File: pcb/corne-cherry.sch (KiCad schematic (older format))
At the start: 146 parts, among them J1 MJ-4PP-9, J2 OLED, J3 MJ-4PP-9, J4 OLED, J5 Conn_01x01_Male, J6 Conn_01x01_Male, P1 Conn_01x03, P3 Conn_01x03, SW1 SW_PUSH, SW10 SW_PUSH, SW11 SW_PUSH, SW12 SW_PUSH, SW13 SW_PUSH, SW14 SW_PUSH, SW15 SW_PUSH, SW16 SW_PUSH, SW17 SW_PUSH, SW18 SW_PUSH, SW19 SW_PUSH, SW2 SW_PUSH, SW20 SW_PUSH, SW21 SW_PUSH, SW22 SW_PUSH, SW23 SW_PUSH, SW24 SW_PUSH, SW25 SW_PUSH, SW26 SW_PUSH, SW27 SW_PUSH, SW28 SW_PUSH, SW29 SW_PUSH, SW3 SW_PUSH, SW30 SW_PUSH, SW31 SW_PUSH, SW32 SW_PUSH, SW33 SW_PUSH, SW34 SW_PUSH, SW35 SW_PUSH, SW36 SW_PUSH, SW37 SW_PUSH, SW38 SW_PUSH, SW39 SW_PUSH, SW4 SW_PUSH, SW40 SW_PUSH, SW41 SW_PUSH, SW42 SW_PUSH, SW43 Rotary_Encoder_Switch, SW44 Rotary_Encoder_Switch, SW5 SW_PUSH, SW6 SW_PUSH, SW7 SW_PUSH, SW8 SW_PUSH, SW9 SW_PUSH, U1 ProMicro, U2 ProMicro

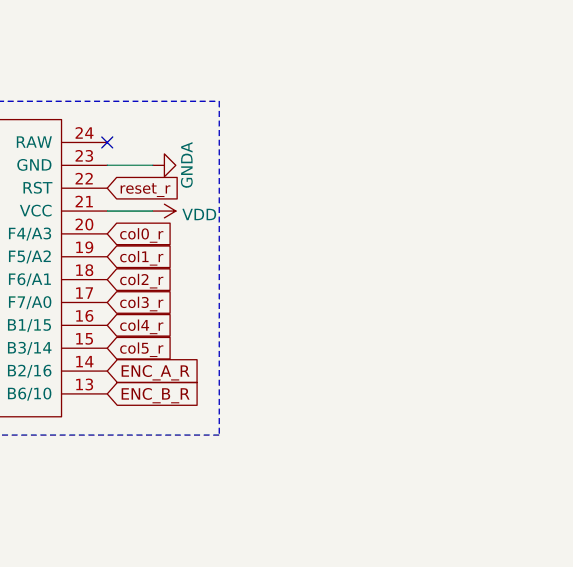
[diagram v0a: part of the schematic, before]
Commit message: added pimoroni
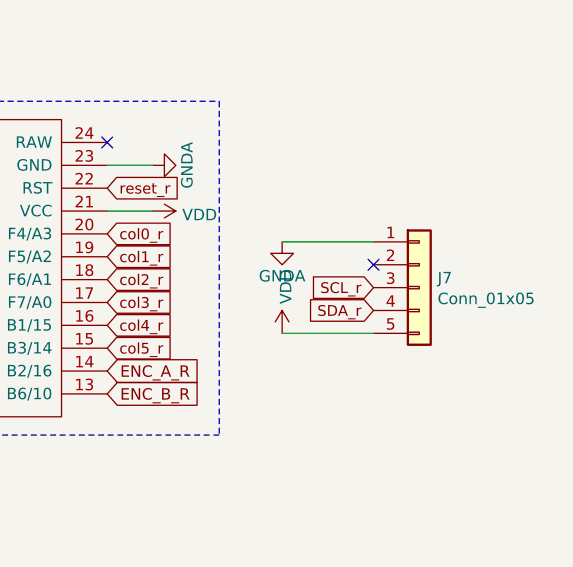
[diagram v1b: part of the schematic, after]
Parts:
- added J7: Conn_01x05, other_parts:pimoroni-trackballl-bommod, symbol Connector_Generic:Conn_01x05
- R1, R2: footprint Resistor_THT:R_Axial_DIN0207_L6.3mm_D2.5mm_P7.62mm_Horizontal -> Resistor_SMD:R_0805_2012Metric
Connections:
- net GNDA: now also J7.1 (Pin_1)
- net SCL_r: now also J7.3 (Pin_3)
- net SDA_r: now also J7.4 (Pin_4)
- net VDD: now also J7.5 (Pin_5)
- no-connect marks 8 -> 9
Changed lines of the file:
@@
 Text GLabel 6700 3105 0    60   Input ~ 0
 reset_r
-NoConn ~ 11285 1715
 Text GLabel 12685 2015 2    47   Input ~ 0
 col0_r
@@
 F 0 "R1" H 3374 2496 50  0000 L CNN
 F 1 "4.7k" H 3374 2405 50  0000 L CNN
-F 2 "Resistor_THT:R_Axial_DIN0207_L6.3mm_D2.5mm_P7.62mm_Horizontal" H 3315 2450 50  0001 C CNN
+F 2 "Resistor_SMD:R_0805_2012Metric" H 3315 2450 50  0001 C CNN
 F 3 "~" H 3315 2450 50  0001 C CNN
 	1    3315 2450
@@
 F 0 "R2" H 3769 2501 50  0000 L CNN
 F 1 "4.7k" H 3769 2410 50  0000 L CNN
-F 2 "Resistor_THT:R_Axial_DIN0207_L6.3mm_D2.5mm_P7.62mm_Horizontal" H 3710 2455 50  0001 C CNN
+F 2 "Resistor_SMD:R_0805_2012Metric" H 3710 2455 50  0001 C CNN
 F 3 "~" H 3710 2455 50  0001 C CNN
 	1    3710 2455
@@
 Wire Wire Line
 	5080 10400 4870 10400
+$Comp
+L Connector_Generic:Conn_01x05 J7
+U 1 1 60A7901D
+P 14050 2250
+F 0 "J7" H 14130 2292 50  0000 L CNN
+F 1 "Conn_01x05" H 14130 2201 50  0000 L CNN
+F 2 "other_parts:pimoroni-trackballl-bommod" H 14050 2250 50  0001 C CNN
+F 3 "~" H 14050 2250 50  0001 C CNN
+	1    14050 2250
+	1    0    0    -1
+$EndComp
+Text GLabel 13850 2350 0    47   Input ~ 0
+SDA_r
+Text GLabel 13850 2250 0    47   Input ~ 0
+SCL_r
+NoConn ~ 11285 1715
+NoConn ~ 13850 2150
+$Comp
+L power:GNDA #PWR?
+U 1 1 60D45B45
+P 13450 2050
+F 0 "#PWR?" H 13450 1800 50  0001 C CNN
+F 1 "GNDA" H 13450 1900 50  0000 C CNN
+F 2 "" H 13450 2050 50  0001 C CNN
+F 3 "" H 13450 2050 50  0001 C CNN
+	1    13450 2050
+	1    0    0    -1
+$EndComp
+Wire Wire Line
+	13450 2050 13850 2050
+$Comp
+L power:VDD #PWR?
+U 1 1 60D5F654
+P 13450 2450
+F 0 "#PWR?" H 13450 2300 50  0001 C CNN
+F 1 "VDD" V 13467 2578 50  0000 L CNN
+F 2 "" H 13450 2450 50  0001 C CNN
+F 3 "" H 13450 2450 50  0001 C CNN
+	1    13450 2450
+	1    0    0    -1
+$EndComp
+Wire Wire Line
+	13450 2450 13850 2450
 $EndSCHEMATC
